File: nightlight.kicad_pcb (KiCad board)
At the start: 2 copper layers, 58.4 x 50.8 mm, 44 parts, among them J1 Conn_01x06_Pin, SW1 SKRTLAE010, SW2 SKRTLAE010, SW3 SW_Push, SW4 SW_Push, U1 ESP-12F, U2 USB-TYPE-C-009, U4 AMS1117-3.3

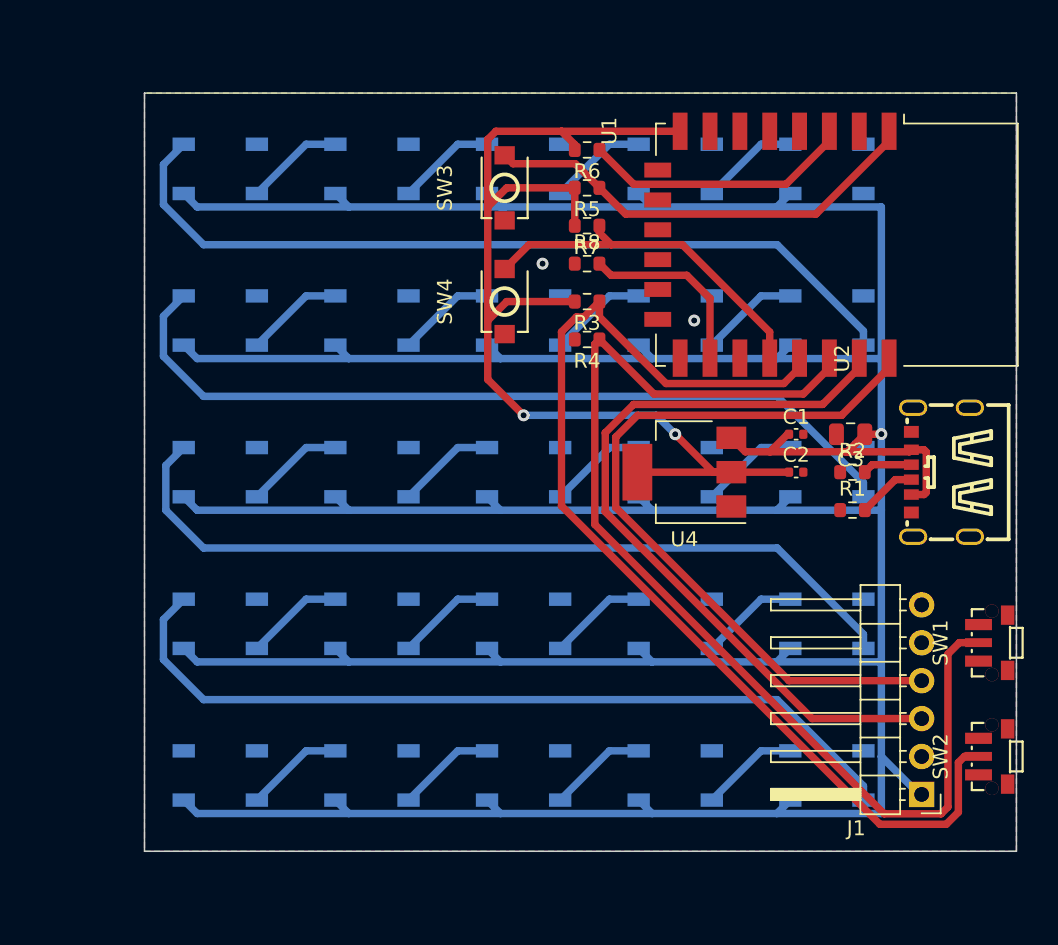
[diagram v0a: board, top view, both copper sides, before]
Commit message: Rearrange front side Add images, readme
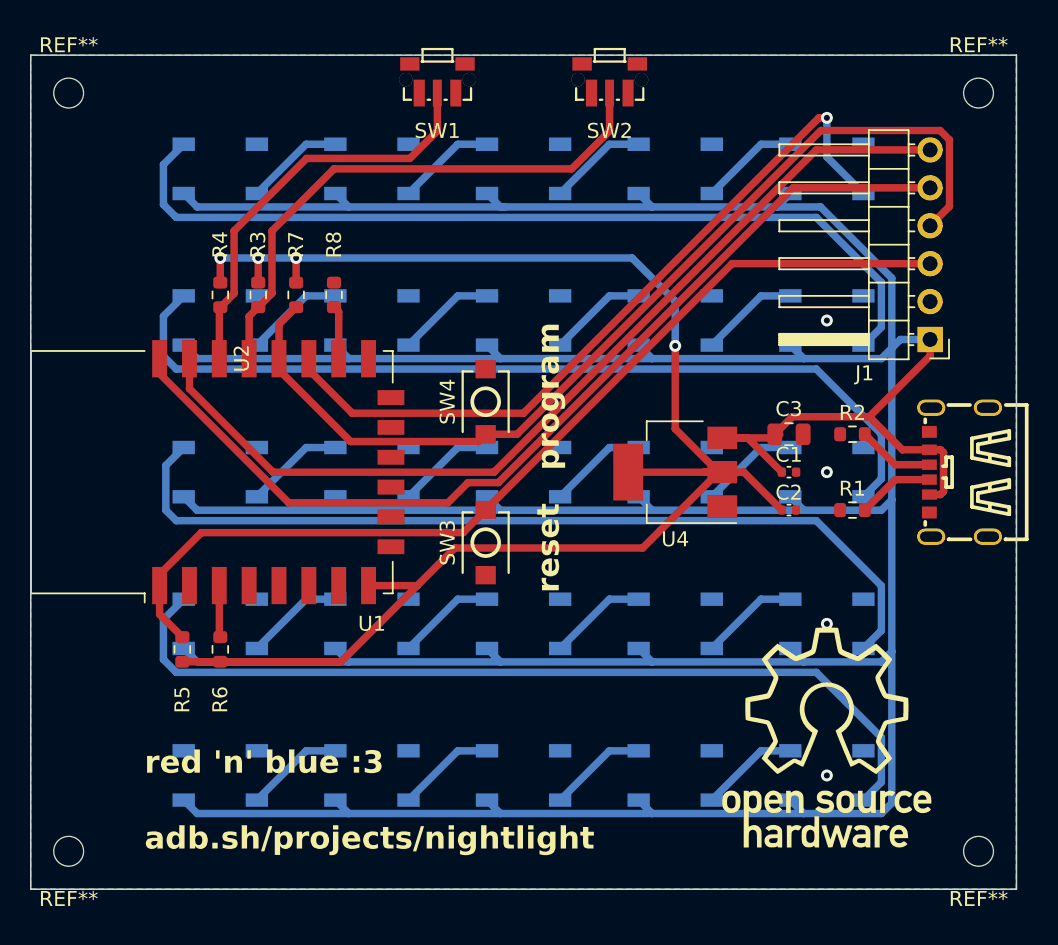
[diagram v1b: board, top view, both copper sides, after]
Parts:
- added G***: LOGO, LOGO, F.Cu at (96.5, 94.0)
- added REF**: MountingHole_2mm, MountingHole:MountingHole_2mm, F.Cu at (106.7, 101.6)
- added REF**: MountingHole_2mm, MountingHole:MountingHole_2mm, F.Cu at (45.7, 101.6)
- added REF**: MountingHole_2mm, MountingHole:MountingHole_2mm, F.Cu at (45.7, 50.8)
- added REF**: MountingHole_2mm, MountingHole:MountingHole_2mm, F.Cu at (106.7, 50.8)
- moved SW1 53.1 mm to (70.4, 49.8), turned to 180 degrees
- moved SW2 52.2 mm to (82.0, 49.8), turned to 180 degrees
- moved U1 44.6 mm to (55.3, 76.2), turned to 90 degrees
- moved R6 41.5 mm to (55.9, 88.1), turned to -90 degrees
- moved R5 41.1 mm to (53.3, 88.1), turned to -90 degrees
- moved J1 30.5 mm to (103.4, 67.3)
- moved R4 24.8 mm to (55.9, 64.3), turned to 90 degrees
- moved SW3 23.8 mm to (73.7, 80.9), turned to -90 degrees
- moved R3 22.0 mm to (58.4, 64.3), turned to 90 degrees
- moved R7 20.0 mm to (61.0, 64.3), turned to 90 degrees
- moved R8 17.1 mm to (63.5, 64.3), turned to -90 degrees
- moved SW4 6.83 mm to (73.7, 71.5), turned to -90 degrees
- moved C3 4.13 mm to (94.0, 73.7), turned to 0 degrees
- moved C1 2.58 mm to (94.0, 76.2)
- moved C2 2.58 mm to (94.0, 78.7)
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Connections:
- J1 pad 3: /RX -> /reset
- J1 pad 4: /TX -> /program
- J1 pad 5: /program -> /TX
- J1 pad 6: /reset -> /RX
- SW3 pad 1: GND -> /reset
- SW3 pad 2: /reset -> GND
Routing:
- net /neopixels: track 0.00 -> 51.1 mm, vias 0 -> 1
- net /SW2: track 75.3 -> 27.9 mm
- net /program: track 24.2 -> 66.8 mm
- net /SW1: track 73.0 -> 37.1 mm
- net /reset: track 30.1 -> 65.1 mm
- net +3V3: track 75.1 -> 108.1 mm, vias 2 -> 4
- net /TX: track 50.9 -> 65.7 mm
- net Net-(U1-EN): track 18.2 -> 3.48 mm
- net /RX: track 51.7 -> 62.9 mm
- net +5V: track 327.7 -> 338.1 mm, vias 1 -> 0
- net Net-(U1-GPIO15): track 12.4 -> 3.58 mm
- net Net-(D20-DOUT): track 56.0 -> 59.6 mm
- net Net-(D5-DOUT): track 56.0 -> 59.6 mm
- net Net-(D15-DOUT): track 55.8 -> 59.4 mm
- net Net-(D10-DOUT): track 56.0 -> 59.6 mm
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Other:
- board size 58.4 x 50.8 mm -> 66 x 55.9 mm
- board text added: "adb.sh/projects/nightlight"
- board text added: "program"
- board text added: "red 'n' blue :3"
- board text added: "reset"

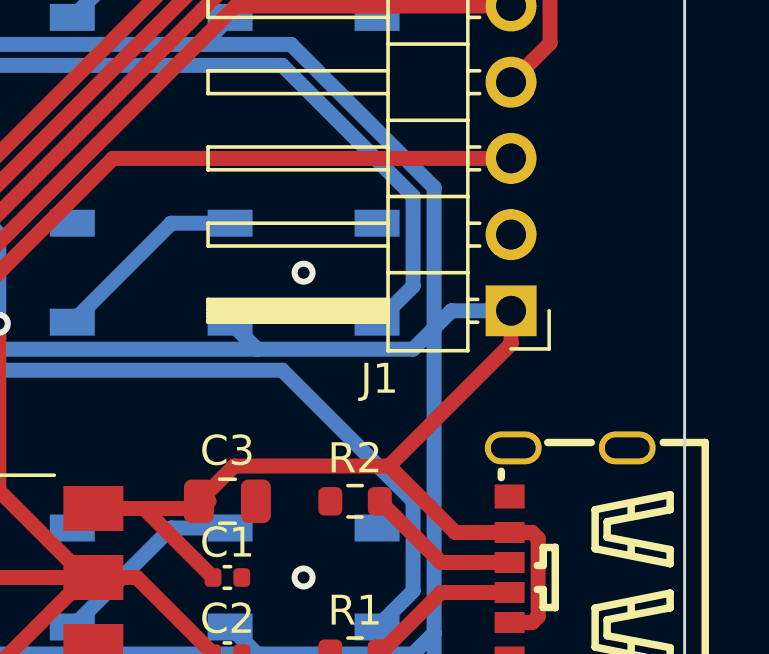
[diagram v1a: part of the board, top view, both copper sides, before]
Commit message: flip gnd and 5v on flash pins
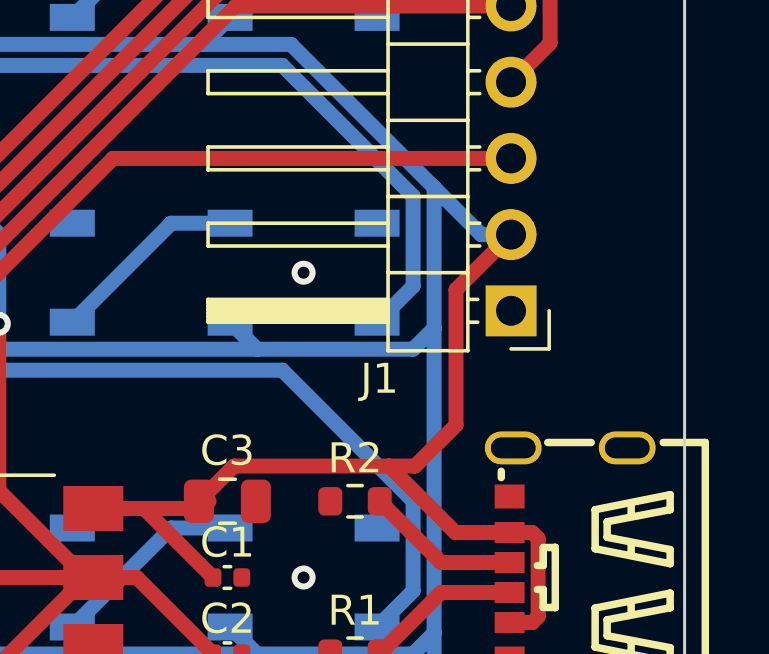
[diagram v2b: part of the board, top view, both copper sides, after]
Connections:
- J1 pad 1: +5V -> GND
- J1 pad 2: GND -> +5V
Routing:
- net +5V: track 338.1 -> 341.6 mm
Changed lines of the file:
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@@
       (stroke (width 0.1) (type solid)) (layer "F.Fab"))
     (pad "1" thru_hole rect (at 0 0 180) (size 1.7 1.7) (drill 1) (layers "*.Cu" "*.Mask")
-      (net 1 "+5V") (pinfunction "Pin_1") (pintype "passive"))
+      (net 3 "GND") (pinfunction "Pin_1") (pintype "passive"))
     (pad "2" thru_hole oval (at 0 2.54 180) (size 1.7 1.7) (drill 1) (layers "*.Cu" "*.Mask")
-      (net 3 "GND") (pinfunction "Pin_2") (pintype "passive"))
+      (net 1 "+5V") (pinfunction "Pin_2") (pintype "passive"))
     (pad "3" thru_hole oval (at 0 5.08 180) (size 1.7 1.7) (drill 1) (layers "*.Cu" "*.Mask")
       (net 17 "/reset") (pinfunction "Pin_3") (pintype "passive"))
@@
   (segment (start 99.365 72.485) (end 94.205 72.485) (width 0.5) (layer "F.Cu") (net 1))
   (segment (start 104.138474 74.7) (end 104.338474 74.9) (width 0.5) (layer "F.Cu") (net 1))
-  (segment (start 103.435 68.415) (end 103.435 67.31) (width 0.5) (layer "F.Cu") (net 1))
   (segment (start 103.388474 74.7) (end 104.138474 74.7) (width 0.5) (layer "F.Cu") (net 1))
   (segment (start 104.338474 77.5) (end 104.138474 77.7) (width 0.5) (layer "F.Cu") (net 1))
+  (segment (start 101.6 66.605) (end 103.435 64.77) (width 0.5) (layer "F.Cu") (net 1))
   (segment (start 91.2 73.9) (end 89.51 73.9) (width 0.5) (layer "F.Cu") (net 1))
-  (segment (start 99.365 72.485) (end 103.435 68.415) (width 0.5) (layer "F.Cu") (net 1))
+  (segment (start 99.365 72.485) (end 100.235 72.485) (width 0.5) (layer "F.Cu") (net 1))
   (segment (start 93.5 76.2) (end 91.2 73.9) (width 0.5) (layer "F.Cu") (net 1))
   (segment (start 94.205 72.485) (end 93.03 73.66) (width 0.5) (layer "F.Cu") (net 1))
   (segment (start 93.13 73.9) (end 93.37 73.66) (width 0.5) (layer "F.Cu") (net 1))
   (segment (start 101.58 74.7) (end 103.388474 74.7) (width 0.5) (layer "F.Cu") (net 1))
+  (segment (start 100.235 72.485) (end 101.6 71.12) (width 0.5) (layer "F.Cu") (net 1))
+  (segment (start 101.6 71.12) (end 101.6 66.605) (width 0.5) (layer "F.Cu") (net 1))
   (segment (start 99.365 72.485) (end 101.58 74.7) (width 0.5) (layer "F.Cu") (net 1))
   (segment (start 92.79 73.9) (end 93.03 73.66) (width 0.5) (layer "F.Cu") (net 1))
@@
   (segment (start 100.17 99.07) (end 94.97 99.07) (width 0.5) (layer "B.Cu") (net 1))
   (segment (start 54.33 68.59) (end 53.43 67.69) (width 0.5) (layer "B.Cu") (net 1))
+  (segment (start 102.439949 64.77) (end 103.435 64.77) (width 0.5) (layer "B.Cu") (net 1))
   (segment (start 84.81 78.75) (end 94.97 78.75) (width 0.5) (layer "B.Cu") (net 1))
-  (segment (start 103.435 67.31) (end 101.45 67.31) (width 0.5) (layer "B.Cu") (net 1))
   (segment (start 100.17 78.75) (end 94.97 78.75) (width 0.5) (layer "B.Cu") (net 1))
   (segment (start 64.49 78.75) (end 54.33 78.75) (width 0.5) (layer "B.Cu") (net 1))
+  (segment (start 100.87 63.200051) (end 102.439949 64.77) (width 0.5) (layer "B.Cu") (net 1))
   (segment (start 64.49 99.07) (end 54.33 99.07) (width 0.5) (layer "B.Cu") (net 1))
   (segment (start 100.87 78.05) (end 100.17 78.75) (width 0.5) (layer "B.Cu") (net 1))
@@
   (segment (start 64.49 68.59) (end 63.59 67.69) (width 0.5) (layer "B.Cu") (net 1))
   (segment (start 94.97 68.59) (end 94.07 67.69) (width 0.5) (layer "B.Cu") (net 1))
-  (segment (start 101.45 67.31) (end 100.87 67.89) (width 0.5) (layer "B.Cu") (net 1))
   (segment (start 84.81 88.91) (end 94.97 88.91) (width 0.5) (layer "B.Cu") (net 1))
   (segment (start 54.33 99.07) (end 53.43 98.17) (width 0.5) (layer "B.Cu") (net 1))

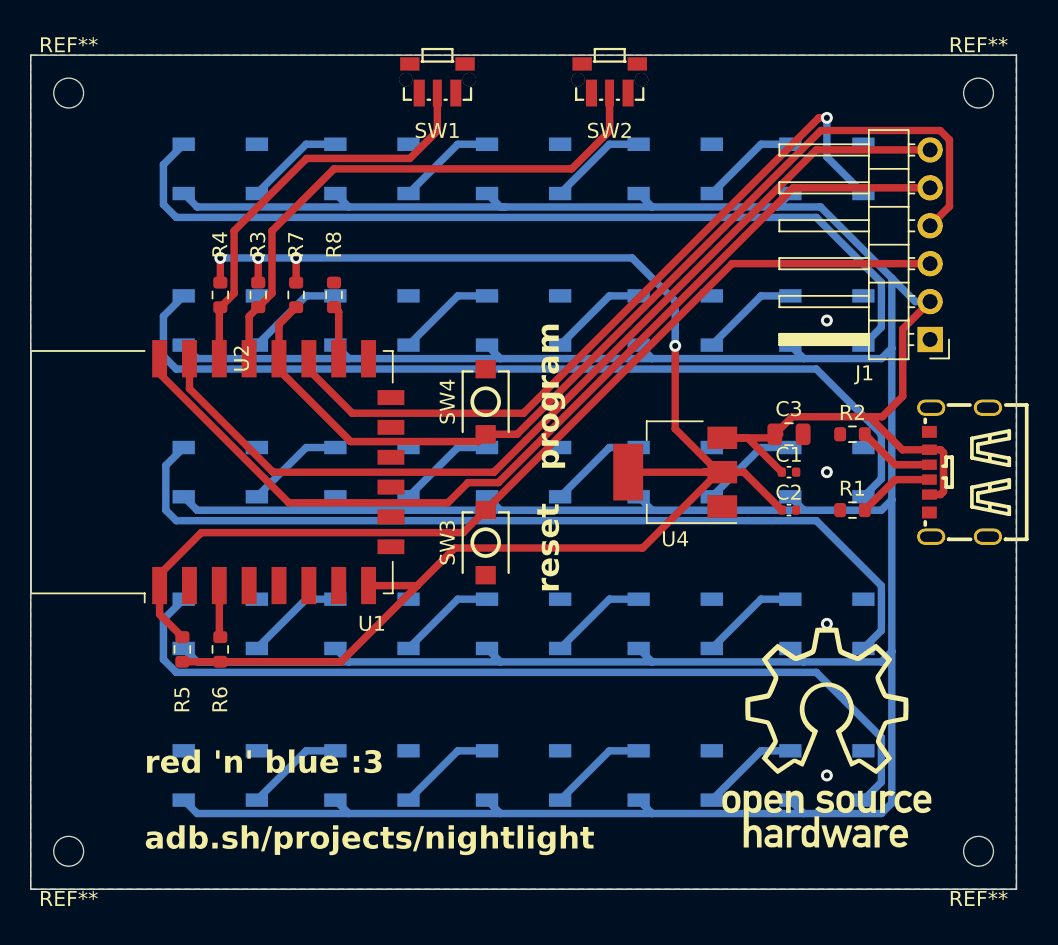
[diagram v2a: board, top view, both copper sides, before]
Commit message: Add C4, C5 Remove J1 Add pads for flashing Add level shifter
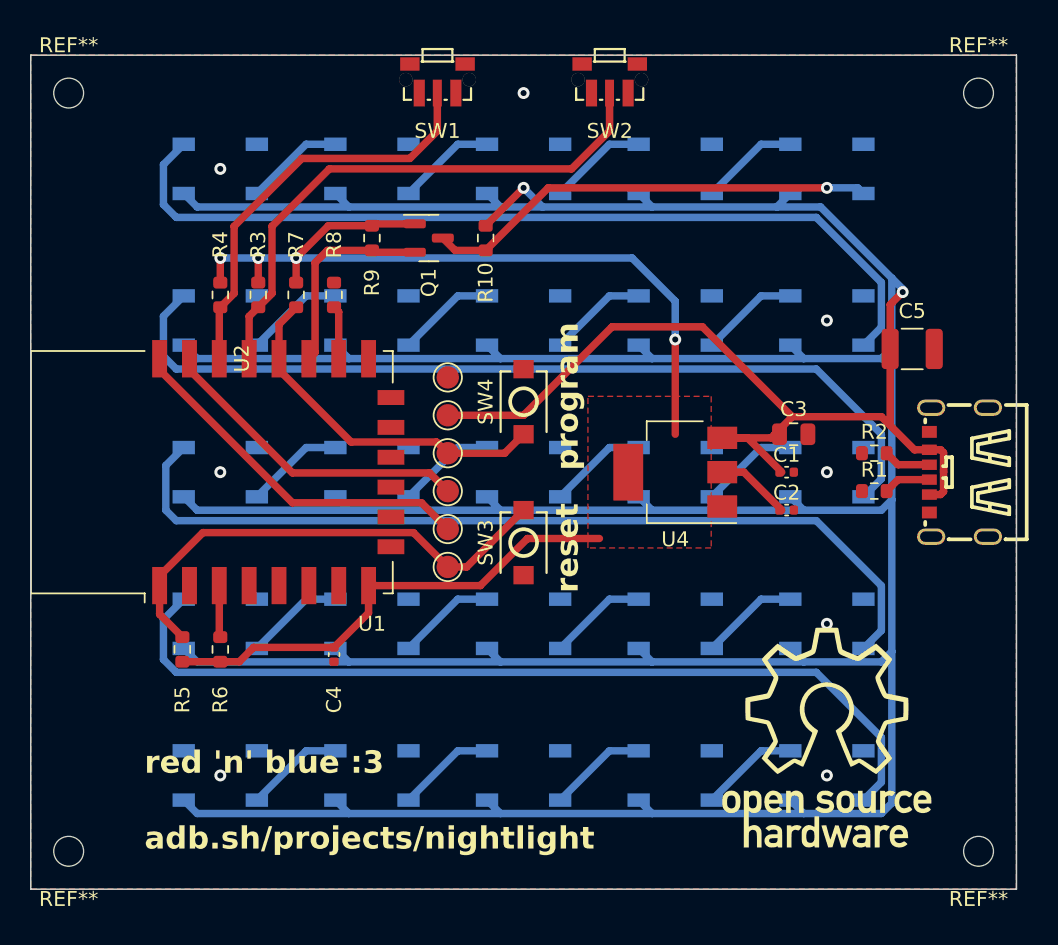
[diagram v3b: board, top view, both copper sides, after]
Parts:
- removed J1: Conn_01x06_Pin, Connector_PinHeader_2.54mm:PinHeader_1x06_P2.54mm_Horizontal
- added C4: 100nF, Capacitor_SMD:C_0402_1005Metric, F.Cu at (63.5, 88.4)
- added C5: 100uF, Capacitor_SMD:C_1210_3225Metric, F.Cu at (102.2, 67.9)
- added Q1: BSS138, Package_TO_SOT_SMD:SOT-23, F.Cu at (69.8, 60.5)
- added R10: R, Resistor_SMD:R_0603_1608Metric, F.Cu at (73.7, 60.5)
- added R9: R, Resistor_SMD:R_0603_1608Metric, F.Cu at (66.0, 60.5)
- added TP1: TestPoint, TestPoint:TestPoint_Pad_D1.5mm, F.Cu at (71.1, 69.8)
- added TP2: TestPoint, TestPoint:TestPoint_Pad_D1.5mm, F.Cu at (71.1, 72.4)
- added TP3: TestPoint, TestPoint:TestPoint_Pad_D1.5mm, F.Cu at (71.1, 82.5)
- added TP4: TestPoint, TestPoint:TestPoint_Pad_D1.5mm, F.Cu at (71.1, 74.9)
- added TP5: TestPoint, TestPoint:TestPoint_Pad_D1.5mm, F.Cu at (71.1, 80.0)
- added TP6: TestPoint, TestPoint:TestPoint_Pad_D1.5mm, F.Cu at (71.1, 77.5)
- C1, C2: value C -> 100nF
- C3: value C -> 10uF
- moved SW3 2.54 mm to (76.2, 80.9)
- moved SW4 2.54 mm to (76.2, 71.5)
- moved R2 1.94 mm to (99.7, 74.9)
- moved R1 1.94 mm to (99.7, 77.5)
- moved C3 0.31 mm to (94.3, 73.7)
- moved C1 0.16 mm to (93.8, 76.2)
- moved C2 0.16 mm to (93.8, 78.7)
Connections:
- D1 pad 4: /neopixels -> Net-(D1-DIN)
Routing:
- net /program: track 66.8 -> 23.9 mm
- net /RX: track 62.9 -> 21.4 mm
- net /TX: track 65.7 -> 24.5 mm
- net /neopixels: track 51.1 -> 13.7 mm, vias 1 -> 0
- net /reset: track 65.1 -> 32.9 mm
- net +5V: track 341.6 -> 372.3 mm, vias 0 -> 2
- net Net-(D1-DIN): track 0.00 -> 30.5 mm, vias 0 -> 1
- net +3V3: track 108.1 -> 93.9 mm
- net Net-(U2-CC2): track 5.17 -> 3.19 mm
- net Net-(U2-CC1): track 5.17 -> 3.19 mm
- net GND: vias 4 -> 8
- added copper zone on F.Cu, net +3V3
